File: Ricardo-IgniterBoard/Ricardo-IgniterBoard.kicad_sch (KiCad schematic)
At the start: 39 parts, among them J1 RBUS, U1 ESP32-S3, Y1 R940000171

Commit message: Auto stash before merge of "icl-rocketry/main" and "main"
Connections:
- net Nuke0: now also U1.38 (GPIO33); no longer U1.40 (GPIO35)
- net Nuke2: now also U1.40 (GPIO35); no longer U1.38 (GPIO33)

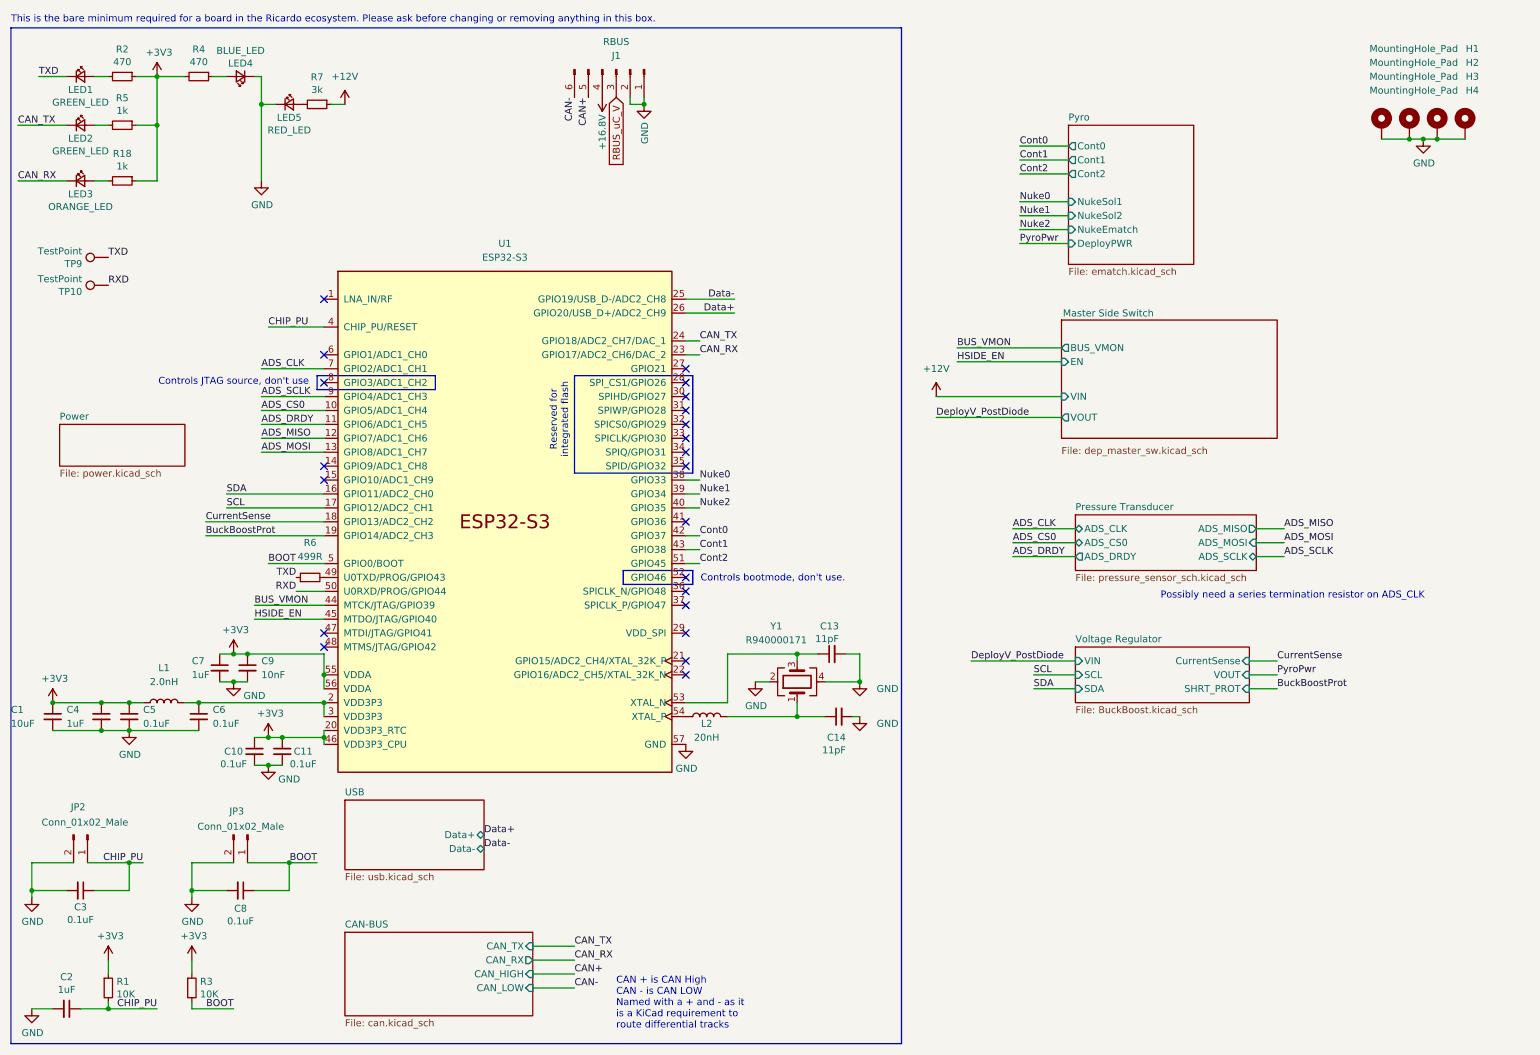
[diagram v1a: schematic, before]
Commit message: Assigning components
And added the thermocouple
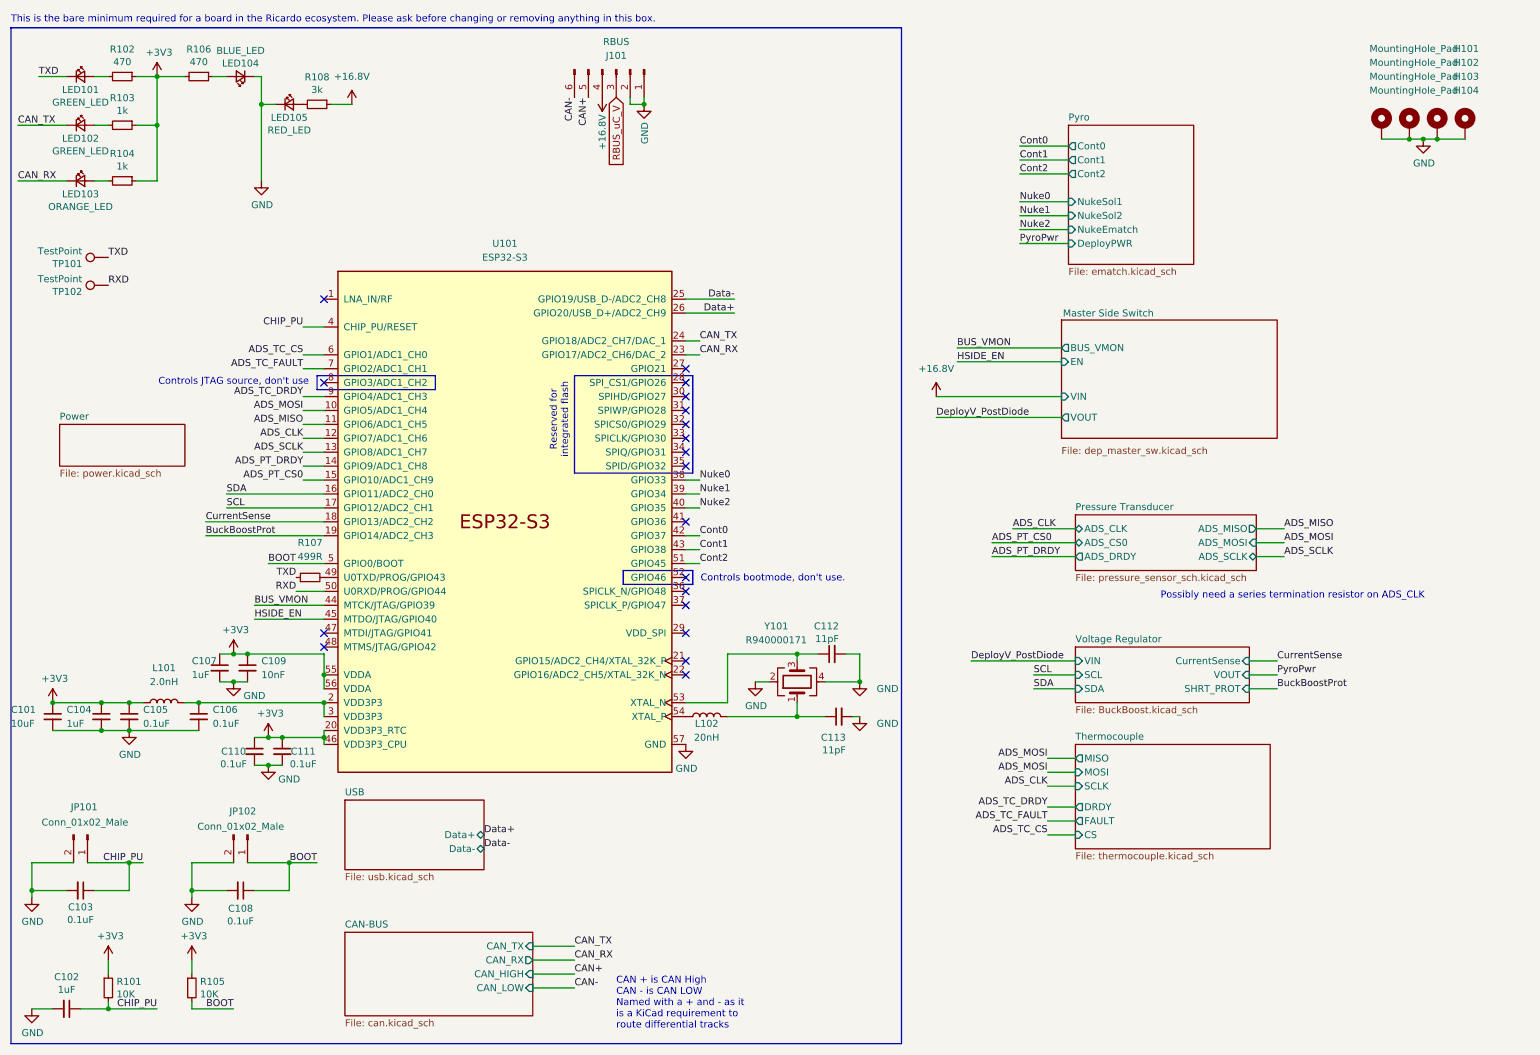
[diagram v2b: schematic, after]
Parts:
- renumbered C1 to C101, C2 to C102, C3 to C103, C4 to C104, C5 to C105, C6 to C106, C7 to C107, C8 to C108, C9 to C109, C10 to C110, C11 to C111, C13 to C112, C14 to C113, H1 to H101, H2 to H102, H3 to H103, H4 to H104, J1 to J101, JP2 to JP101, JP3 to JP102, L1 to L101, L2 to L102, LED1 to LED101, LED2 to LED102, LED3 to LED103, LED4 to LED104, LED5 to LED105, R1 to R101, R2 to R102, R5 to R103, R18 to R104, R3 to R105, R4 to R106, R6 to R107, R7 to R108, TP9 to TP101, TP10 to TP102, U1 to U101, Y1 to Y101
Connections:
- net +12V is gone; now on net +16.8V: R108.1
- net ADS_CS0 is gone; now on net ADS_MOSI: U101.10 (GPIO5/ADC1_CH4)
- net ADS_DRDY is gone; now on net ADS_MISO: U101.11 (GPIO6/ADC1_CH5)
- net ADS_CLK: now also U101.12 (GPIO7/ADC1_CH6); no longer U101.7 (GPIO2/ADC1_CH1)
- net ADS_MISO: no longer U101.12 (GPIO7/ADC1_CH6)
- net ADS_MOSI: no longer U101.13 (GPIO8/ADC1_CH7)
- net ADS_SCLK: now also U101.13 (GPIO8/ADC1_CH7); no longer U101.9 (GPIO4/ADC1_CH3)
- net ADS_PT_DRDY: now reaches U101.14 (GPIO9/ADC1_CH8)
- net ADS_PT_CS0: now reaches U101.15 (GPIO10/ADC1_CH9)
- net ADS_TC_CS: now reaches U101.6 (GPIO1/ADC1_CH0)
- new net ADS_TC_DRDY: U101.9 (GPIO4/ADC1_CH3)
- new net ADS_TC_FAULT: U101.7 (GPIO2/ADC1_CH1)
- no-connect marks 22 -> 19
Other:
- added sheet Thermocouple (thermocouple.kicad_sch)

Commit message: Fixed tc and igniter power
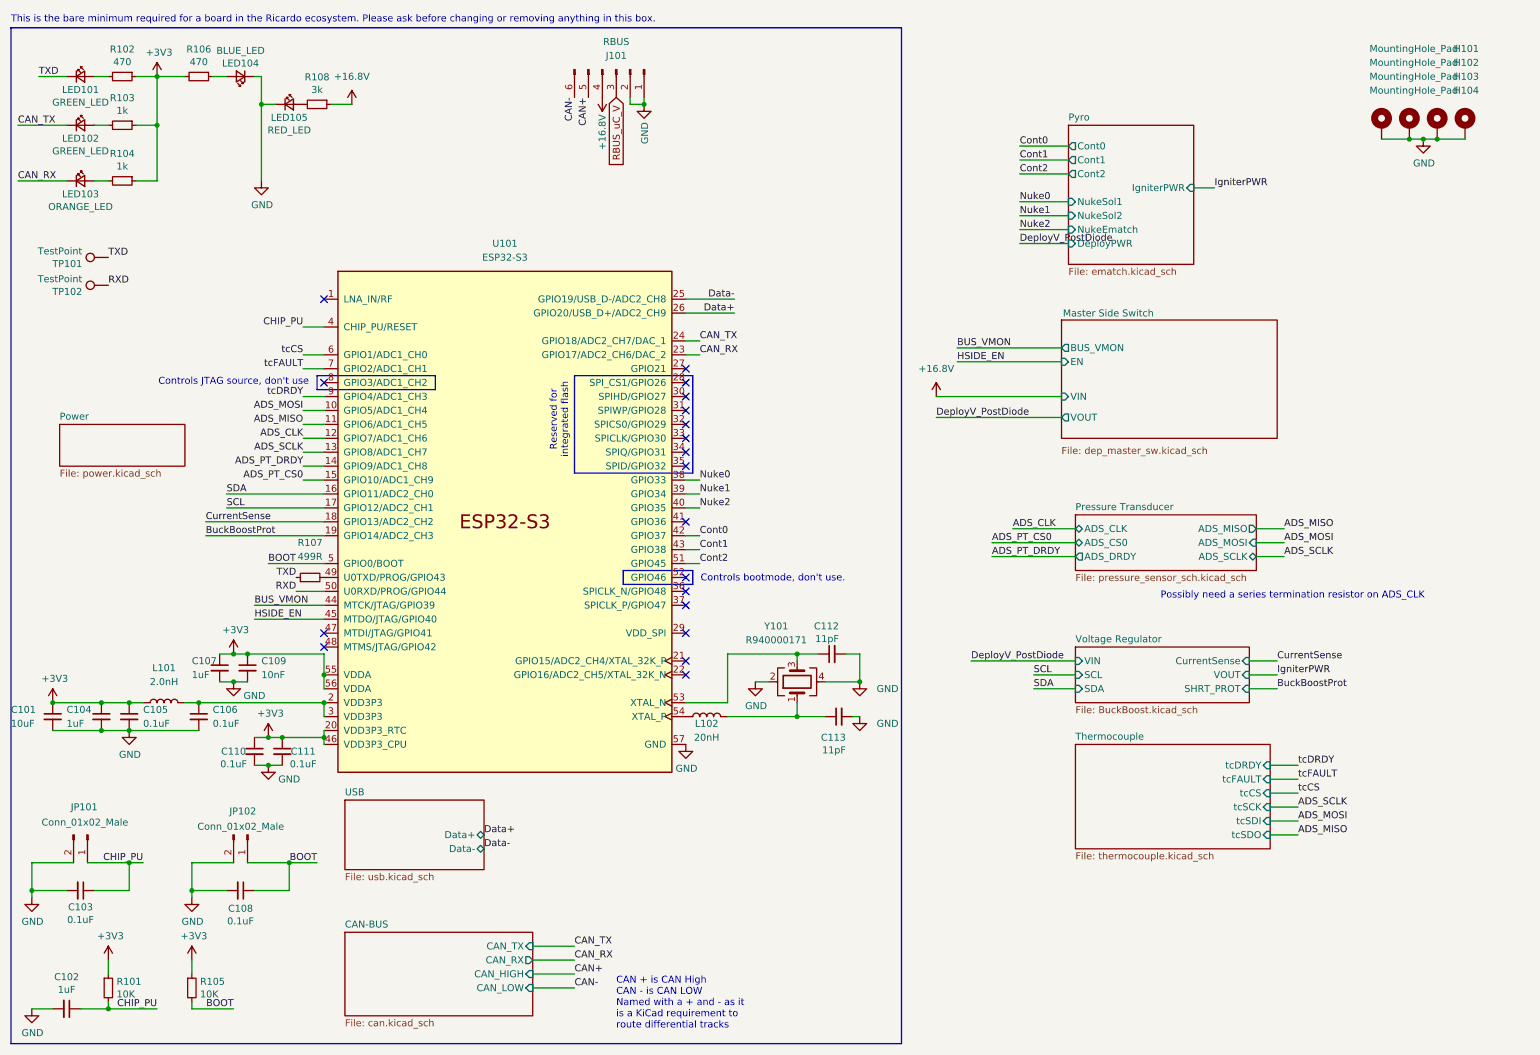
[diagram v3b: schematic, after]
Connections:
- net ADS_TC_CS renamed tcCS
- net ADS_TC_DRDY renamed tcDRDY
- net ADS_TC_FAULT renamed tcFAULT
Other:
- sheet Pyro ports: added IgniterPWR; removed none
- sheet Thermocouple ports: added tcCS, tcDRDY, tcFAULT, tcSCK, tcSDI, tcSDO; removed CS, DRDY, FAULT, MISO, MOSI, SCLK
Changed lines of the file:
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@@
 	(wire
 		(pts
+			(xy 242.57 149.86) (xy 247.65 149.86)
+		)
+		(stroke
+			(width 0)
+			(type default)
+		)
+	)
+	(wire
+		(pts
 			(xy 29.21 135.89) (xy 34.29 135.89)
 		)
@@
 	(wire
 		(pts
+			(xy 242.57 152.4) (xy 247.65 152.4)
+		)
+		(stroke
+			(width 0)
+			(type default)
+		)
+	)
+	(wire
+		(pts
 			(xy 267.97 33.02) (xy 262.89 33.02)
 		)
@@
 	(wire
 		(pts
-			(xy 201.93 151.13) (xy 207.01 151.13)
+			(xy 27.94 21.59) (xy 30.48 21.59)
 		)
 		(stroke
@@
 	(wire
 		(pts
-			(xy 27.94 21.59) (xy 30.48 21.59)
+			(xy 204.47 80.01) (xy 181.61 80.01)
 		)
 		(stroke
@@
 	(wire
 		(pts
-			(xy 204.47 80.01) (xy 181.61 80.01)
+			(xy 16.51 165.1) (xy 16.51 170.18)
 		)
 		(stroke
@@
 	(wire
 		(pts
-			(xy 16.51 165.1) (xy 16.51 170.18)
+			(xy 161.29 132.08) (xy 167.64 132.08)
 		)
 		(stroke
@@
 	(wire
 		(pts
-			(xy 161.29 132.08) (xy 167.64 132.08)
+			(xy 228.6 41.91) (xy 232.41 41.91)
 		)
 		(stroke
@@
 	(wire
 		(pts
-			(xy 201.93 157.48) (xy 207.01 157.48)
-		)
-		(stroke
-			(width 0)
-			(type default)
-		)
-	)
-	(wire
-		(pts
 			(xy 199.39 133.35) (xy 207.01 133.35)
 		)
@@
 	(wire
 		(pts
-			(xy 201.93 148.59) (xy 207.01 148.59)
-		)
-		(stroke
-			(width 0)
-			(type default)
-		)
-	)
-	(wire
-		(pts
 			(xy 107.95 187.96) (xy 115.57 187.96)
 		)
@@
 	(wire
 		(pts
-			(xy 201.93 146.05) (xy 207.01 146.05)
+			(xy 185.42 73.66) (xy 204.47 73.66)
 		)
 		(stroke
@@
 	(wire
 		(pts
-			(xy 185.42 73.66) (xy 204.47 73.66)
+			(xy 242.57 154.94) (xy 247.65 154.94)
 		)
 		(stroke
@@
 	(wire
 		(pts
+			(xy 242.57 157.48) (xy 247.65 157.48)
+		)
+		(stroke
+			(width 0)
+			(type default)
+		)
+	)
+	(wire
+		(pts
 			(xy 240.03 109.22) (xy 245.11 109.22)
 		)
@@
 	(wire
 		(pts
-			(xy 201.93 160.02) (xy 207.01 160.02)
-		)
-		(stroke
-			(width 0)
-			(type default)
-		)
-	)
-	(wire
-		(pts
 			(xy 181.61 83.82) (xy 204.47 83.82)
 		)
@@
 	(wire
 		(pts
+			(xy 242.57 147.32) (xy 247.65 147.32)
+		)
+		(stroke
+			(width 0)
+			(type default)
+		)
+	)
+	(wire
+		(pts
 			(xy 196.85 39.37) (xy 205.74 39.37)
 		)
@@
 	(wire
 		(pts
-			(xy 201.93 154.94) (xy 207.01 154.94)
-		)
-		(stroke
-			(width 0)
-			(type default)
-		)
-	)
-	(wire
-		(pts
 			(xy 59.69 142.24) (xy 62.23 142.24)
 		)
@@
 	(wire
 		(pts
+			(xy 242.57 160.02) (xy 247.65 160.02)
+		)
+		(stroke
+			(width 0)
+			(type default)
+		)
+	)
+	(wire
+		(pts
 			(xy 135.89 105.41) (xy 138.43 105.41)
 		)
@@
 		)
 	)
-	(label "ADS_TC_CS"
-		(at 201.93 160.02 180)
+	(label "tcFAULT"
+		(at 247.65 149.86 0)
 		(effects
 			(font
 				(size 1.27 1.27)
 			)
-			(justify right bottom)
+			(justify left bottom)
 		)
 	)
@@
 		)
 	)
-	(label "ADS_TC_DRDY"
-		(at 201.93 154.94 180)
-		(effects
-			(font
-				(size 1.27 1.27)
-			)
-			(justify right bottom)
-		)
-	)
 	(label "Nuke1"
 		(at 196.85 46.99 0)
@@
 		)
 	)
+	(label "ADS_MOSI"
+		(at 247.65 157.48 0)
+		(effects
+			(font
+				(size 1.27 1.27)
+			)
+			(justify left bottom)
+		)
+	)
+	(label "tcDRDY"
+		(at 247.65 147.32 0)
+		(effects
+			(font
+				(size 1.27 1.27)
+			)
+			(justify left bottom)
+		)
+	)
 	(label "CAN+"
 		(at 115.57 185.42 0)
@@
 		)
 	)
+	(label "tcCS"
+		(at 247.65 152.4 0)
+		(effects
+			(font
+				(size 1.27 1.27)
+			)
+			(justify left bottom)
+		)
+	)
 	(label "Data+"
 		(at 99.06 160.02 0)
@@
 		)
 	)
-	(label "ADS_MOSI"
-		(at 201.93 146.05 180)
-		(effects
-			(font
-				(size 1.27 1.27)
-			)
-			(justify right bottom)
-		)
-	)
 	(label "BuckBoostProt"
 		(at 48.26 105.41 0)
@@
 		)
 	)
-	(label "ADS_TC_CS"
+	(label "tcCS"
 		(at 66.04 72.39 180)
 		(effects
@@
 		)
 	)
-	(label "ADS_TC_FAULT"
-		(at 201.93 157.48 180)
-		(effects
-			(font
-				(size 1.27 1.27)
-			)
-			(justify right bottom)
-		)
-	)
 	(label "ADS_PT_DRDY"
 		(at 191.77 109.22 0)
@@
 		)
 	)
-	(label "ADS_TC_FAULT"
+	(label "tcFAULT"
 		(at 66.04 74.93 180)
 		(effects
@@
 		)
 	)
-	(label "ADS_TC_DRDY"
+	(label "ADS_SCLK"
+		(at 247.65 154.94 0)
+		(effects
+			(font
+				(size 1.27 1.27)
+			)
+			(justify left bottom)
+		)
+	)
+	(label "tcDRDY"
 		(at 66.04 80.01 180)
 		(effects
@@
 		)
 	)
-	(label "CAN_RX"
-		(at 115.57 182.88 0)
+	(label "ADS_MISO"
+		(at 247.65 160.02 0)
 		(effects
 			(font
@@
 		)
 	)
-	(label "ADS_CLK"
-		(at 201.93 151.13 180)
+	(label "CAN_RX"
+		(at 115.57 182.88 0)
 		(effects
 			(font
 				(size 1.27 1.27)
 			)
-			(justify right bottom)
+			(justify left bottom)
 		)
 	)
@@
 		)
 	)
-	(label "PyroPwr"
+	(label "IgniterPWR"
+		(at 232.41 41.91 0)
+		(effects
+			(font
+				(size 1.27 1.27)
+			)
+			(justify left bottom)
+		)
+	)
+	(label "IgniterPWR"
 		(at 243.84 130.81 0)
 		(effects
@@
 		)
 	)
-	(label "PyroPwr"
+	(label "DeployV_PostDiode"
 		(at 196.85 52.07 0)
 		(effects
@@
 		)
 	)
-	(label "ADS_MOSI"
-		(at 201.93 148.59 180)
-		(effects
-			(font
-				(size 1.27 1.27)
-			)
-			(justify right bottom)
-		)
-	)
 	(global_label "RBUS_uC_V"
 		(shape input)
@@
 			)
 		)
-		(pin "CS" input
-			(at 207.01 160.02 180)
+		(pin "tcDRDY" input
+			(at 242.57 147.32 0)
 			(effects
 				(font
 					(size 1.27 1.27)
 				)
-				(justify left)
+				(justify right)
 			)
 		)
-		(pin "DRDY" output
-			(at 207.01 154.94 180)
+		(pin "tcFAULT" input
+			(at 242.57 149.86 0)
 			(effects
 				(font
 					(size 1.27 1.27)
 				)
-				(justify left)
+				(justify right)
 			)
 		)
-		(pin "FAULT" output
-			(at 207.01 157.48 180)
+		(pin "tcCS" input
+			(at 242.57 152.4 0)
 			(effects
 				(font
 					(size 1.27 1.27)
 				)
-				(justify left)
+				(justify right)
 			)
 		)
-		(pin "MISO" output
-			(at 207.01 146.05 180)
+		(pin "tcSCK" input
+			(at 242.57 154.94 0)
 			(effects
 				(font
 					(size 1.27 1.27)
 				)
-				(justify left)
+				(justify right)
 			)
 		)
-		(pin "MOSI" input
-			(at 207.01 148.59 180)
+		(pin "tcSDI" input
+			(at 242.57 157.48 0)
 			(effects
 				(font
 					(size 1.27 1.27)
 				)
-				(justify left)
+				(justify right)
 			)
 		)
-		(pin "SCLK" input
-			(at 207.01 151.13 180)
+		(pin "tcSDO" input
+			(at 242.57 160.02 0)
 			(effects
 				(font
 					(size 1.27 1.27)
 				)
-				(justify left)
+				(justify right)
 			)
 		)
@@
 			)
 		)
+		(pin "IgniterPWR" input
+			(at 228.6 41.91 0)
+			(effects
+				(font
+					(size 1.27 1.27)
+				)
+				(justify right)
+			)
+		)
